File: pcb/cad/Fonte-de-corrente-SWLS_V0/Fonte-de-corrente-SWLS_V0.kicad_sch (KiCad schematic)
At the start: 32 parts, among them J2 LEMO FFA.0S, J3 LEMO FFA.0S, J4 Barrel_Jack_Switch, SW1 SW_DPDT_x2, U1 LM78L05, U2 LT3080xST, U3 LT3092xST, U4 LT3092xST, U5 74AHC1G04, U6 TS5A21366, U7 TS5A21366, U8 TS5A21366, U9 TS5A21366

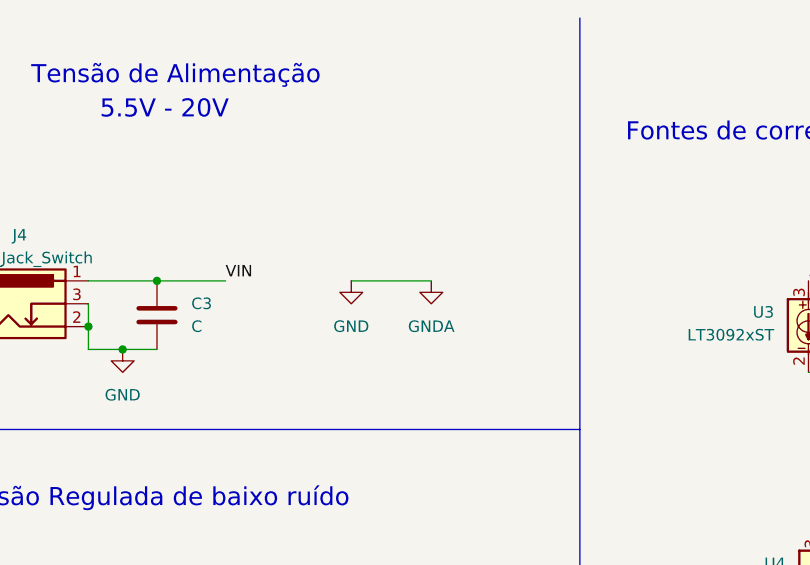
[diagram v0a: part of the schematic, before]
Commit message: Atualização do layout de PCB para revisão
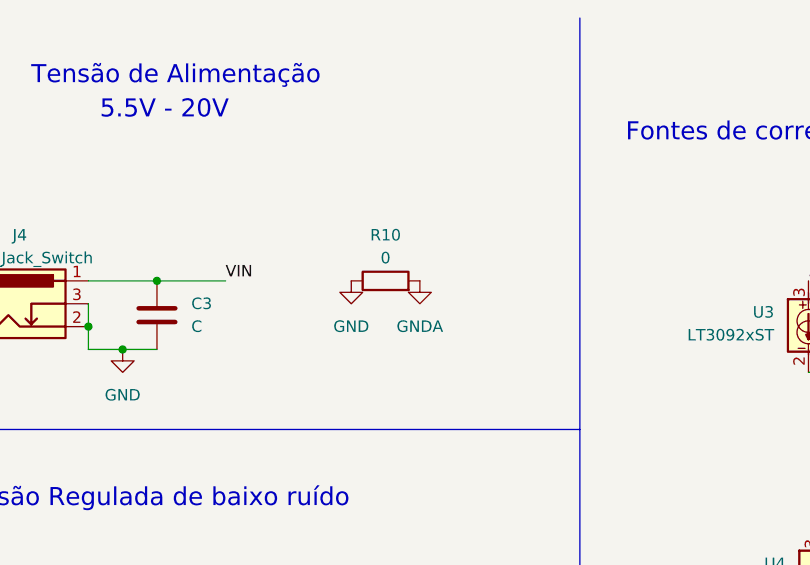
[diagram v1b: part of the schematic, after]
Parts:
- added R10: 0, Resistor_SMD:R_0805_2012Metric, symbol Device:R
- J2, J3: footprint Fonte-de-corrente-SWLS-complementar:Lemo_Painel_4vias -> Fonte-de-corrente-SWLS-complementar:EPG.0B.302.HLN; Numero do produto (none) -> EPG.0B.304.HLN
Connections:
- net GND: now also R10.1; no longer C5.2, U6.5 (NO2), U7.5 (NO2), U8.1 (NO1), U9.1 (NO1)
- new net GNDA: C5.2, R10.2, U6.5 (NO2), U7.5 (NO2), U8.1 (NO1), U9.1 (NO1)
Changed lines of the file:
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@@
-    (stroke (width 0) (type default))
-  )
-  (wire (pts (xy 76.2 41.91) (xy 85.09 41.91))
     (stroke (width 0) (type default))
   )
@@
       (effects (font (size 1.27 1.27)))
     )
-    (property "Footprint" "Fonte-de-corrente-SWLS-complementar:Lemo_Painel_4vias" (at 259.08 146.05 0)
-      (effects (font (size 1.27 1.27)) hide)
-    )
-    (property "Datasheet" " ~" (at 259.08 146.05 0)
+    (property "Footprint" "Fonte-de-corrente-SWLS-complementar:EPG.0B.302.HLN" (at 259.08 146.05 0)
+      (effects (font (size 1.27 1.27)) hide)
+    )
+    (property "Datasheet" " https://br.mouser.com/datasheet/2/232/EPG_0B_304_HLN-1844998.pdf" (at 259.08 146.05 0)
+      (effects (font (size 1.27 1.27)) hide)
+    )
+    (property "Numero do produto" "EPG.0B.304.HLN" (at 259.08 146.05 0)
       (effects (font (size 1.27 1.27)) hide)
     )
@@
         (path "/485d57e1-9e59-4bdb-b543-f102996c1764"
           (reference "R4") (unit 1)
+        )
+      )
+    )
+  )
+  (symbol (lib_id "Device:R") (at 80.01 41.91 90) (unit 1)
+    (in_bom yes) (on_board yes) (dnp no) (fields_autoplaced)
+    (property "Reference" "R10" (at 80.01 36.83 90)
+      (effects (font (size 1.27 1.27)))
+    )
+    (property "Value" "0" (at 80.01 39.37 90)
+      (effects (font (size 1.27 1.27)))
+    )
+    (property "Footprint" "Resistor_SMD:R_0805_2012Metric" (at 80.01 43.688 90)
+      (effects (font (size 1.27 1.27)) hide)
+    )
+    (property "Datasheet" "~" (at 80.01 41.91 0)
+      (effects (font (size 1.27 1.27)) hide)
+    )
+    (pin "1")
+    (pin "2")
+    (instances
+      (project "Fonte-de-corrente-SWLS_V0"
+        (path "/485d57e1-9e59-4bdb-b543-f102996c1764"
+          (reference "R10") (unit 1)
         )
       )
@@
       (effects (font (size 1.27 1.27)))
     )
-    (property "Footprint" "Fonte-de-corrente-SWLS-complementar:Lemo_Painel_4vias" (at 214.63 146.05 0)
-      (effects (font (size 1.27 1.27)) hide)
-    )
-    (property "Datasheet" " ~" (at 214.63 146.05 0)
+    (property "Footprint" "Fonte-de-corrente-SWLS-complementar:EPG.0B.302.HLN" (at 214.63 146.05 0)
+      (effects (font (size 1.27 1.27)) hide)
+    )
+    (property "Datasheet" "https://br.mouser.com/datasheet/2/232/EPG_0B_304_HLN-1844998.pdf" (at 214.63 146.05 0)
+      (effects (font (size 1.27 1.27)) hide)
+    )
+    (property "Numero do produto" "EPG.0B.304.HLN" (at 214.63 146.05 0)
       (effects (font (size 1.27 1.27)) hide)
     )
@@
     )
   )
-  (symbol (lib_id "power:GNDA") (at 85.09 41.91 0) (unit 1)
-    (in_bom yes) (on_board yes) (dnp no) (fields_autoplaced)
-    (property "Reference" "#PWR023" (at 85.09 48.26 0)
-      (effects (font (size 1.27 1.27)) hide)
-    )
-    (property "Value" "GNDA" (at 85.09 46.99 0)
-      (effects (font (size 1.27 1.27)))
-    )
-    (property "Footprint" "" (at 85.09 41.91 0)
-      (effects (font (size 1.27 1.27)) hide)
-    )
-    (property "Datasheet" "" (at 85.09 41.91 0)
-      (effects (font (size 1.27 1.27)) hide)
-    )
+  (symbol (lib_id "power:GNDA") (at 83.82 41.91 0) (unit 1)
+    (in_bom yes) (on_board yes) (dnp no) (fields_autoplaced)
+    (property "Reference" "#PWR023" (at 83.82 48.26 0)
+      (effects (font (size 1.27 1.27)) hide)
+    )
+    (property "Value" "GNDA" (at 83.82 46.99 0)
+      (effects (font (size 1.27 1.27)))
+    )
+    (property "Footprint" "" (at 83.82 41.91 0)
+      (effects (font (size 1.27 1.27)) hide)
+    )
+    (property "Datasheet" "" (at 83.82 41.91 0)
+      (effects (font (size 1.27 1.27)) hide)
+    )

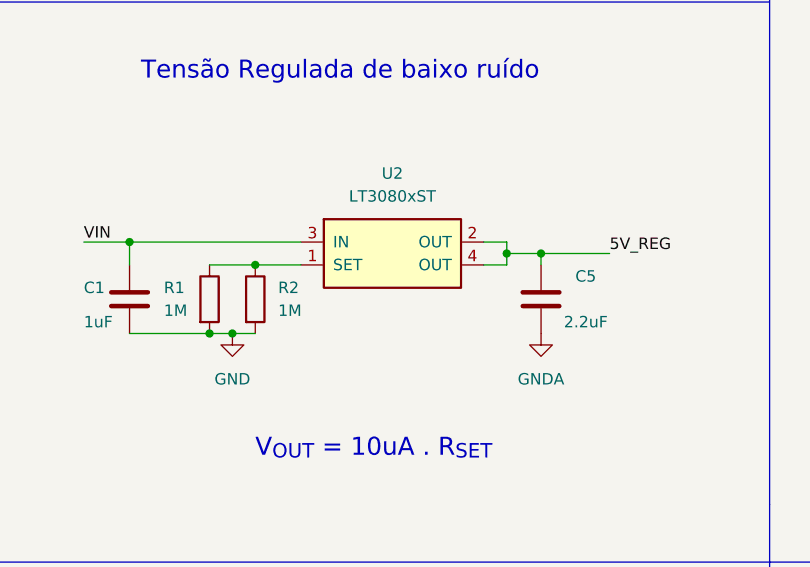
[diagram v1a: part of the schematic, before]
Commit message: Atualização do layout de PCB e esquemático com as correções indicadas nas issues
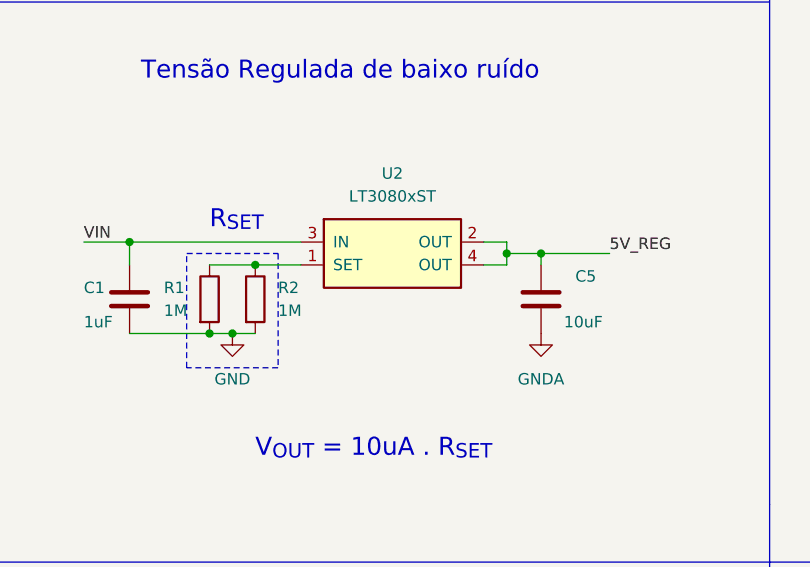
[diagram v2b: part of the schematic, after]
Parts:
- C5: value 2.2uF -> 10uF
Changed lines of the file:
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@@
     (stroke (width 0) (type default))
+  )
+  (rectangle (start 36.83 86.36) (end 46.99 99.06)
+    (stroke (width 0) (type dash))
+    (fill (type none))
   )
   (text "1mA - DC" (at 129.54 31.75 0)
@@
   )
   (text "Acionamento para chaves analógicas " (at 111.76 133.35 0)
+    (effects (font (size 2 2)) (justify left bottom))
+  )
+  (text "R_{SET}" (at 39.37 83.82 0)
     (effects (font (size 2 2)) (justify left bottom))
   )
@@
       (effects (font (size 1.27 1.27)) (justify left))
     )
-    (property "Value" "2.2uF" (at 78.74 93.98 0)
-      (effects (font (size 1.27 1.27)) (justify left))
-    )
+    (property "Value" "10uF" (at 78.74 93.98 0)
+      (effects (font (size 1.27 1.27)) (justify left))
+    )

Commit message: Atualização da ultima versão da PCB e esquemático
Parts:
- C6, C7, C8, C9: footprint Capacitor_SMD:C_0805_2012Metric -> Capacitor_SMD:C_1206_3216Metric
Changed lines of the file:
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@@
       (effects (font (size 1.27 1.27)) (justify left))
     )
-    (property "Footprint" "Capacitor_SMD:C_0805_2012Metric" (at 47.9552 184.15 0)
+    (property "Footprint" "Capacitor_SMD:C_1206_3216Metric" (at 47.9552 184.15 0)
       (effects (font (size 1.27 1.27)) hide)
     )
@@
       (effects (font (size 1.27 1.27)) (justify left))
     )
-    (property "Footprint" "Capacitor_SMD:C_0805_2012Metric" (at 73.3552 184.15 0)
+    (property "Footprint" "Capacitor_SMD:C_1206_3216Metric" (at 73.3552 184.15 0)
       (effects (font (size 1.27 1.27)) hide)
     )
@@
       (effects (font (size 1.27 1.27)) (justify left))
     )
-    (property "Footprint" "Capacitor_SMD:C_0805_2012Metric" (at 60.6552 184.15 0)
+    (property "Footprint" "Capacitor_SMD:C_1206_3216Metric" (at 60.6552 184.15 0)
       (effects (font (size 1.27 1.27)) hide)
     )
@@
       (effects (font (size 1.27 1.27)) (justify left))
     )
-    (property "Footprint" "Capacitor_SMD:C_0805_2012Metric" (at 35.2552 184.15 0)
-      (effects (font (size 1.27 1.27)) hide)
-    )
+    (property "Footprint" "Capacitor_SMD:C_1206_3216Metric" (at 35.2552 184.15 0)
+      (effects (font (size 1.27 1.27)) hide)
+    )
